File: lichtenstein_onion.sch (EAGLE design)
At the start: 40 parts, among them IC1 LM2852Y-3V3, J1 MAGJACK, U1 ONION-OMEGA2

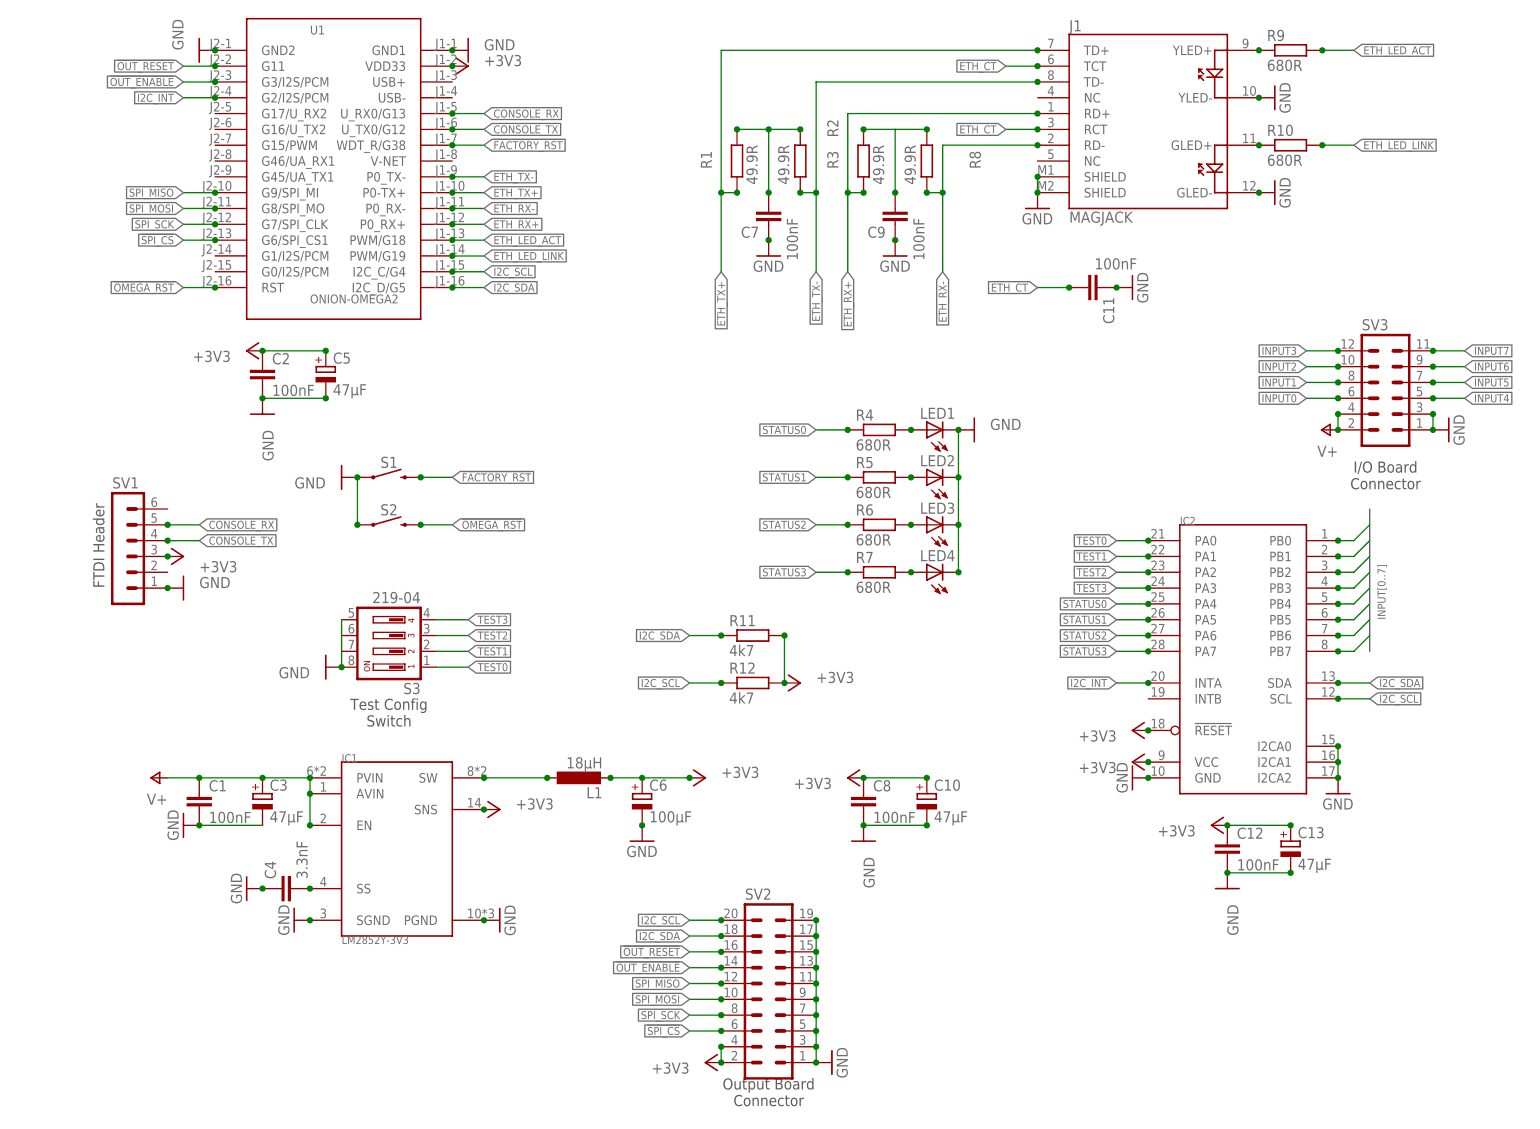
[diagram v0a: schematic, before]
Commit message: Added mouser part numbers for most components
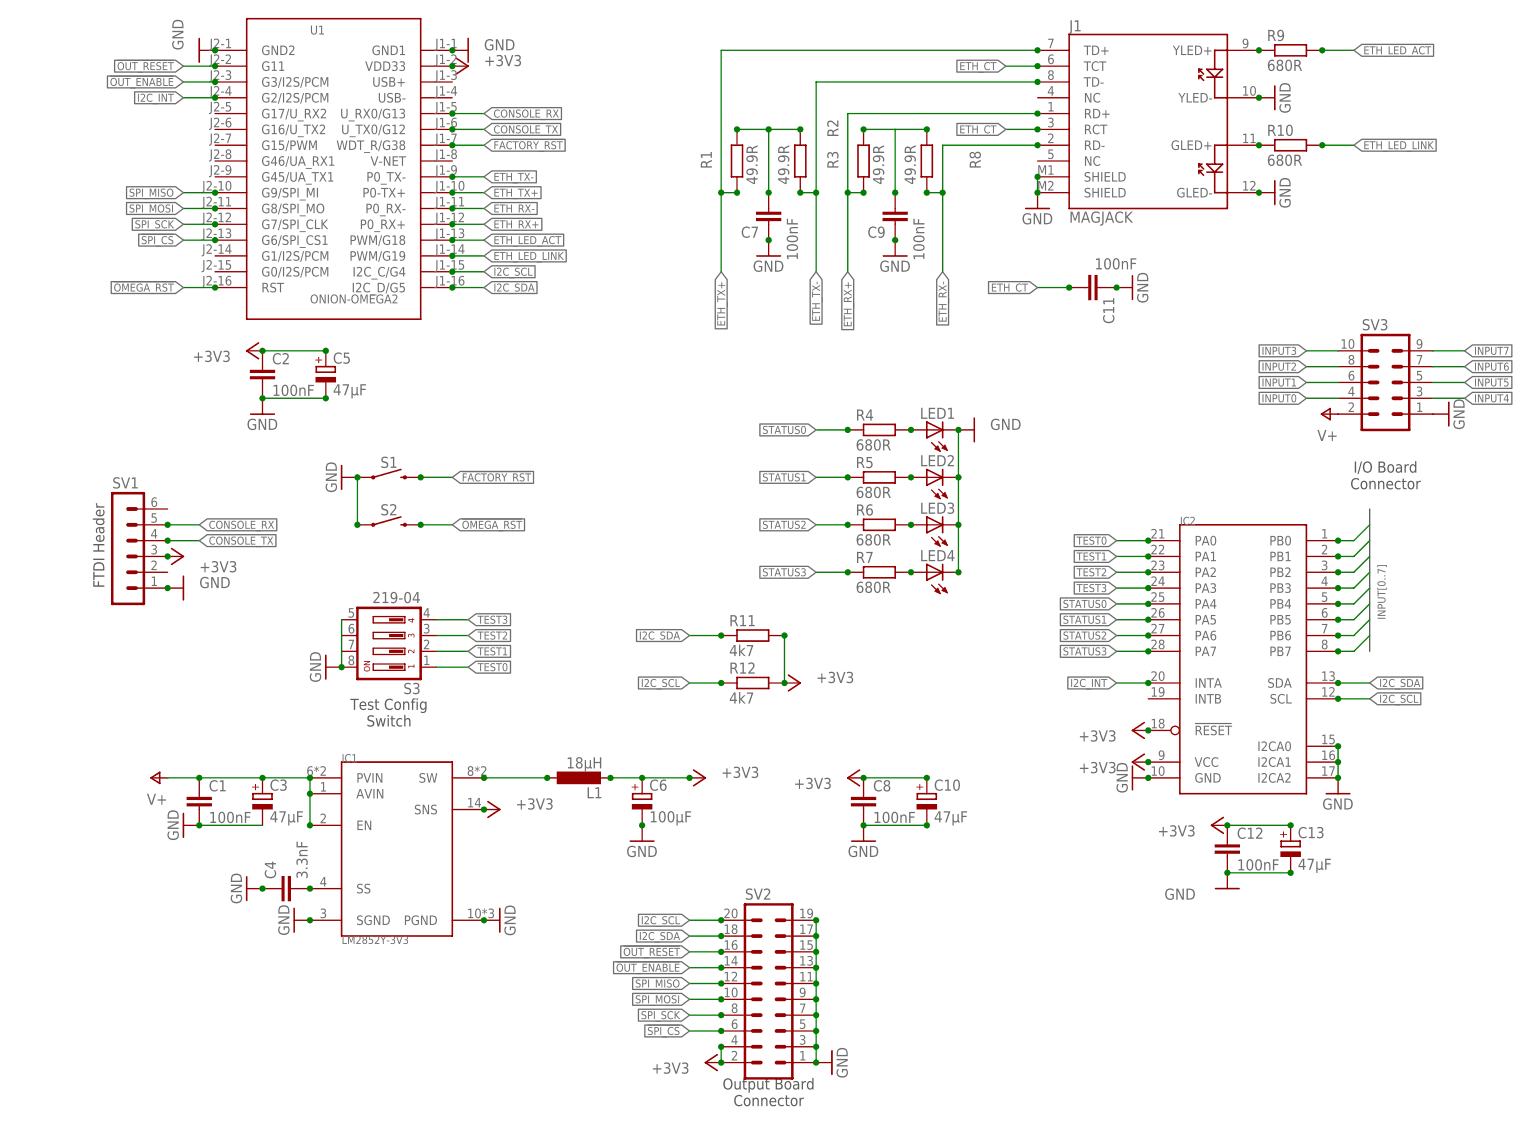
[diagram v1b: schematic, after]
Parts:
- C1, C11, C12, C2, C7, C8, C9: MOUSER (none) -> 710-885012207072
- C4: MOUSER (none) -> 710-885012207089
- L1: MOUSER SRR1050A-180Y -> (none)
- LED1: MOUSER (none) -> 604-APTR3216SRCPRV
- LED2, LED3, LED4: MOUSER (none) -> 604-APTR3216SGC
- R1, R11, R12, R2, R3, R8: MOUSER (none) -> 652-CR0805-FX4701GLF
- R10, R4, R5, R6, R7, R9: MOUSER (none) -> 652-CR0805-FX6800GLF
- S3: MOUSER (none) -> 774-219-4LPS
- SV2: MOUSER (none) -> 517-30320-6002
- SV3: device con-lstb:MA06-2 -> con-lstb:MA05-2; MOUSER (none) -> 517-30310-6002
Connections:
- net GND: no longer SV3.3
- net INPUT0: now also SV3.4; no longer SV3.6
- net INPUT1: now also SV3.6; no longer SV3.8
- net INPUT2: now also SV3.8; no longer SV3.10
- net INPUT3: now also SV3.10; no longer SV3.12
- net INPUT4: now also SV3.3; no longer SV3.5
- net INPUT5: now also SV3.5; no longer SV3.7
- net INPUT6: now also SV3.7; no longer SV3.9
- net INPUT7: now also SV3.9; no longer SV3.11
- net V+: no longer SV3.4

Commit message: began pcb layout for main board
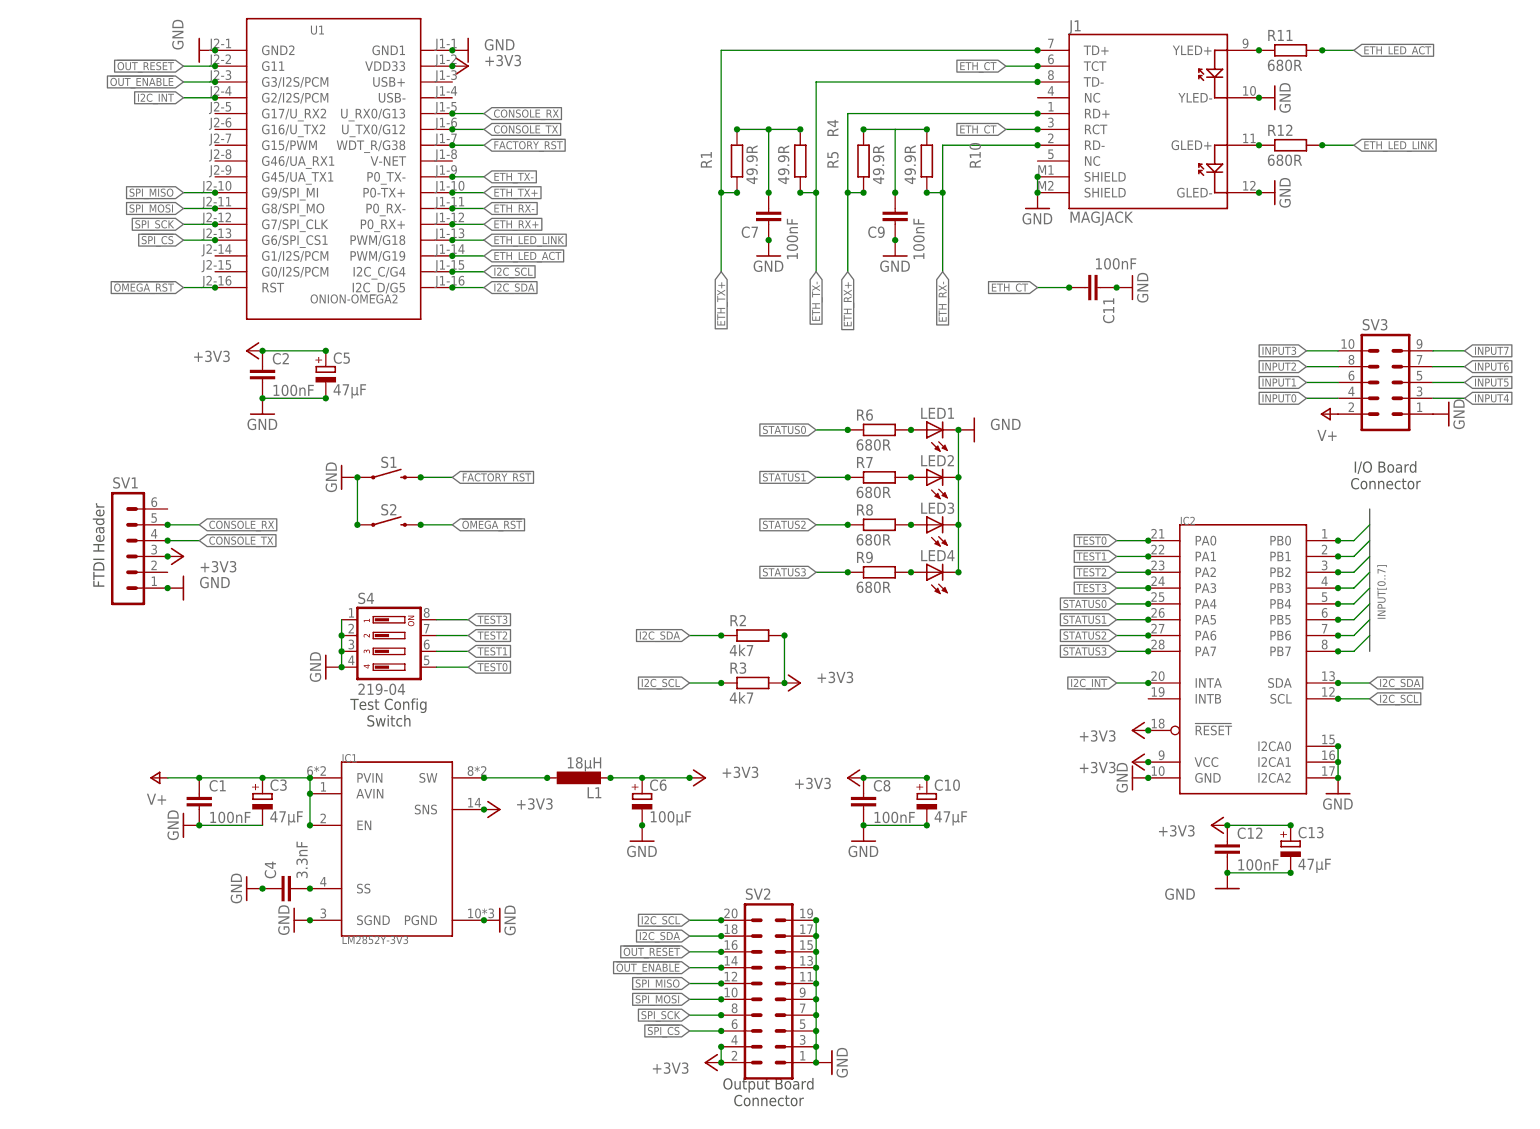
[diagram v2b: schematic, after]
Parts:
- removed S3: 219-04, switch-dil:219-04
- added S4: 219-04, switch-dil:219-04
- R10, R4, R5: value 680R -> 49.9R; MOUSER 652-CR0805-FX6800GLF -> 652-CR0805-FX4701GLF
- R11, R12: value 4k7 -> 680R; MOUSER 652-CR0805-FX4701GLF -> 652-CR0805-FX6800GLF
- R2, R3: value 49.9R -> 4k7
- R8: value 49.9R -> 680R; MOUSER 652-CR0805-FX4701GLF -> 652-CR0805-FX6800GLF
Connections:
- net +3V3: now also R2.2, R3.2; no longer R11.2, R12.2
- net ETH_LED_ACT: now also R11.2, U1.PWM/G19; no longer R9.2, U1.PWM/G18
- net ETH_LED_LINK: now also R12.2, U1.PWM/G18; no longer R10.2, U1.PWM/G19
- net ETH_RX+: now also R5.1; no longer R3.1
- net ETH_RX-: now also R10.1; no longer R8.1
- net ETH_TX-: now also R4.1; no longer R2.1
- net GND: now also S4.1, S4.2, S4.3, S4.4; no longer S3.5, S3.8
- net I2C_SCL: now also R3.1; no longer R12.1
- net I2C_SDA: now also R2.1; no longer R11.1
- net N$10: now also R8.2; no longer R6.2
- net N$11: now also R9.2; no longer R7.2
- net N$2: now also R6.2; no longer R4.2
- net N$3: now also R4.2; no longer R2.2
- net N$4: now also R11.1; no longer R9.1
- net N$5: now also R12.1; no longer R10.1
- net N$6: now also R10.2, R5.2; no longer R3.2, R8.2
- net N$9: now also R7.2; no longer R5.2
- net STATUS0: now also R6.1; no longer R4.1
- net STATUS1: now also R7.1; no longer R5.1
- net STATUS2: now also R8.1; no longer R6.1
- net STATUS3: now also R9.1; no longer R7.1
- net TEST0: now also S4.5; no longer S3.1
- net TEST1: now also S4.6; no longer S3.2
- net TEST2: now also S4.7; no longer S3.3
- net TEST3: now also S4.8; no longer S3.4
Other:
- moved on the sheet: R10, R11, R12, R2, R3, R4, R5, R6, R7, R8, R9

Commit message: finished main board layout
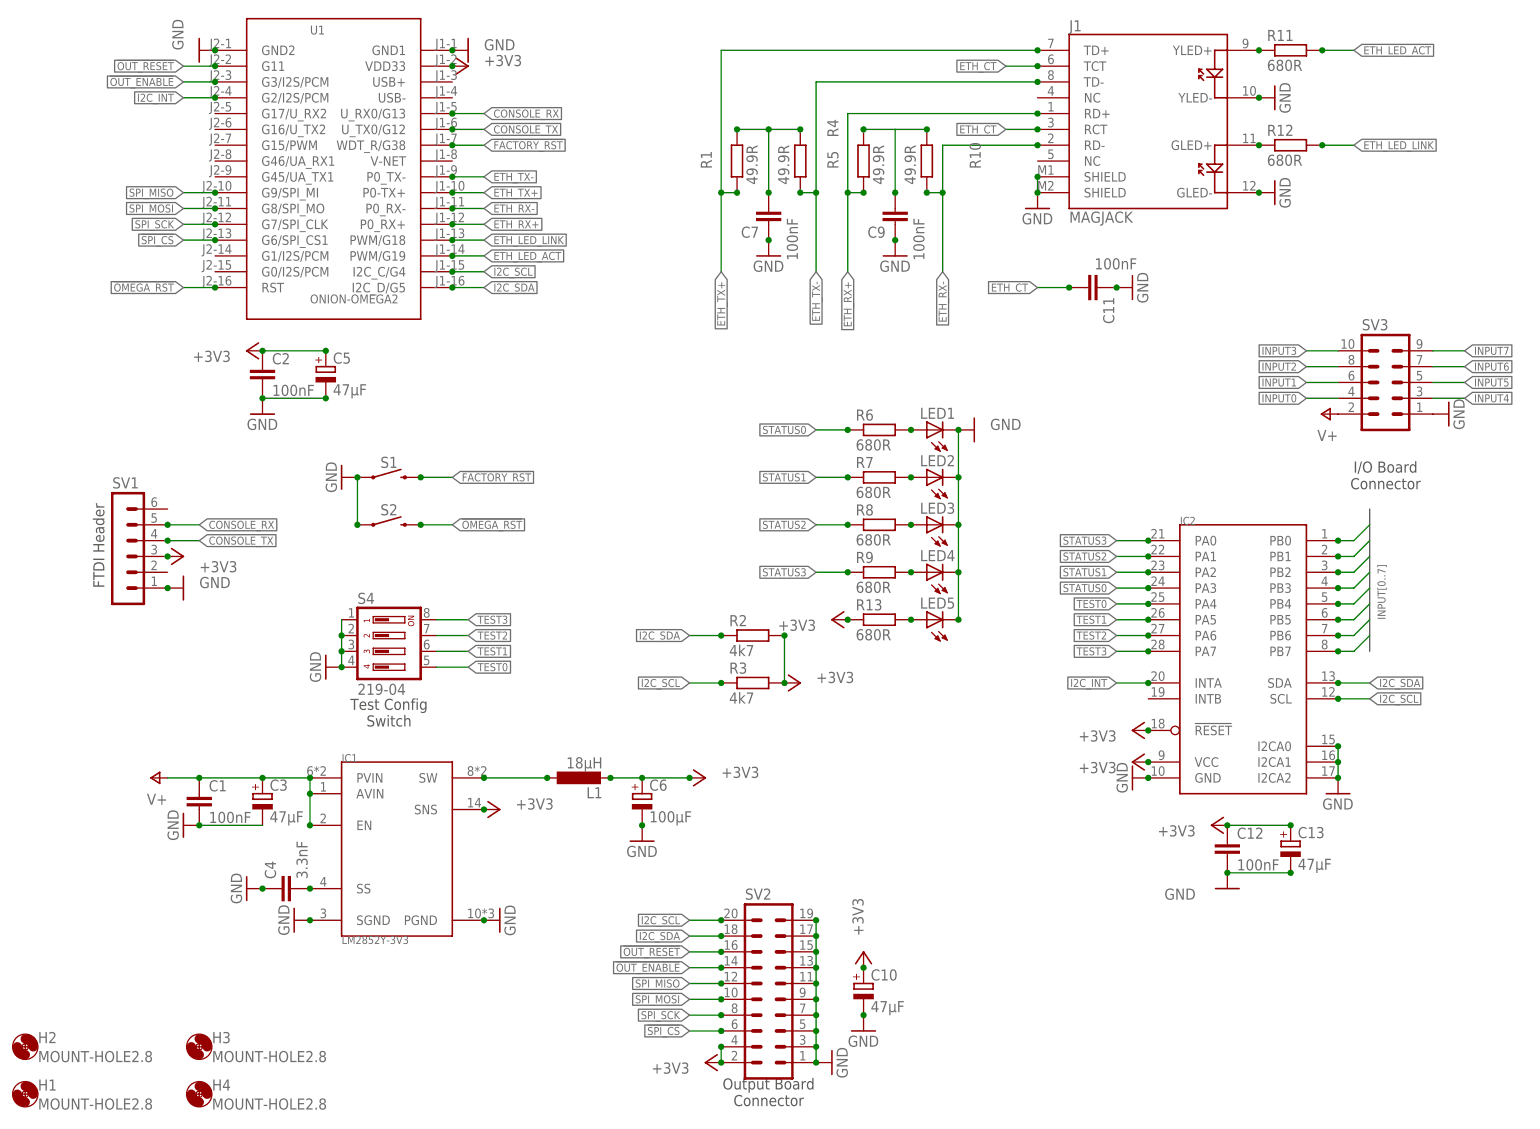
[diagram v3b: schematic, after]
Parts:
- removed C8: 100nF, rcl:C-EUC0805
- added H1, H2, H3, H4: MOUNT-HOLE2.8, holes:MOUNT-HOLE2.8
- added LED5: (no value), led:LEDCHIPLED_1206
- added R13: 680R, rcl:R-EU_M0805
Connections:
- new net N$1: LED5.A, R13.2
- net +3V3: now also R13.1; no longer C8.1
- net GND: now also LED5.C; no longer C8.2
- net INPUT0: now also IC2.PB1; no longer IC2.PB0
- net INPUT1: now also IC2.PB3; no longer IC2.PB1
- net INPUT2: now also IC2.PB5; no longer IC2.PB2
- net INPUT3: now also IC2.PB7; no longer IC2.PB3
- net INPUT4: now also IC2.PB0; no longer IC2.PB4
- net INPUT5: now also IC2.PB2; no longer IC2.PB5
- net INPUT6: now also IC2.PB4; no longer IC2.PB6
- net INPUT7: now also IC2.PB6; no longer IC2.PB7
- net STATUS0: now also IC2.PA3; no longer IC2.PA4
- net STATUS1: now also IC2.PA2; no longer IC2.PA5
- net STATUS2: now also IC2.PA1; no longer IC2.PA6
- net STATUS3: now also IC2.PA0; no longer IC2.PA7
- net TEST0: now also IC2.PA4; no longer IC2.PA0
- net TEST1: now also IC2.PA5; no longer IC2.PA1
- net TEST2: now also IC2.PA6; no longer IC2.PA2
- net TEST3: now also IC2.PA7; no longer IC2.PA3
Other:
- moved on the sheet: C10

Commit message: Rev01 sent to manufacture
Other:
- moved on the sheet: C10, SV2

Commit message: BOM for base board
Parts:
- S1, S2: MOUSER (none) -> 612-TL1105B
- U1: MOUSER (none) -> 353-OM-O2P
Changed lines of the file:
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@@
 <parts>
 <part name="FRAME1" library="frames" library_urn="urn:adsk.eagle:library:229" deviceset="LETTER_L" device=""/>
-<part name="U1" library="lichtenstein_onion" deviceset="ONION-OMEGA2" device=""/>
+<part name="U1" library="lichtenstein_onion" deviceset="ONION-OMEGA2" device="">
+<attribute name="MOUSER" value="353-OM-O2P"/>
+</part>
 <part name="+3V33" library="supply1" library_urn="urn:adsk.eagle:library:371" deviceset="+3V3" device=""/>
 <part name="GND9" library="supply1" library_urn="urn:adsk.eagle:library:371" deviceset="GND" device=""/>
@@
 <part name="GND24" library="supply1" library_urn="urn:adsk.eagle:library:371" deviceset="GND" device=""/>
 <part name="P+2" library="supply1" library_urn="urn:adsk.eagle:library:371" deviceset="V+" device=""/>
-<part name="S1" library="SparkFun-Switches" deviceset="MOMENTARY-SWITCH-SPST" device="-PTH-6.0MM" value=""/>
-<part name="S2" library="SparkFun-Switches" deviceset="MOMENTARY-SWITCH-SPST" device="-PTH-6.0MM" value=""/>
+<part name="S1" library="SparkFun-Switches" deviceset="MOMENTARY-SWITCH-SPST" device="-PTH-6.0MM" value="">
+<attribute name="MOUSER" value="612-TL1105B"/>
+</part>
+<part name="S2" library="SparkFun-Switches" deviceset="MOMENTARY-SWITCH-SPST" device="-PTH-6.0MM" value="">
+<attribute name="MOUSER" value="612-TL1105B"/>
+</part>
 <part name="GND7" library="supply1" library_urn="urn:adsk.eagle:library:371" deviceset="GND" device=""/>
 <part name="LED1" library="led" library_urn="urn:adsk.eagle:library:259" deviceset="LED" device="CHIPLED_1206" package3d_urn="urn:adsk.eagle:package:15823/2">
@@
 <instance part="FRAME1" gate="G$1" x="0" y="0"/>
 <instance part="FRAME1" gate="G$2" x="147.32" y="0"/>
-<instance part="U1" gate="G$1" x="58.42" y="157.48"/>
+<instance part="U1" gate="G$1" x="58.42" y="157.48">
+<attribute name="MOUSER" x="58.42" y="157.48" size="1.27" layer="96" display="off"/>
+</instance>
 <instance part="+3V33" gate="G$1" x="76.2" y="170.18" smashed="yes" rot="R270">
 <attribute name="VALUE" x="78.74" y="170.18" size="1.778" layer="96"/>
@@
 <instance part="GND24" gate="1" x="233.68" y="114.3" rot="R90"/>
 <instance part="P+2" gate="1" x="213.36" y="114.3" rot="R90"/>
-<instance part="S1" gate="G$1" x="63.5" y="104.14"/>
-<instance part="S2" gate="G$1" x="63.5" y="96.52"/>
+<instance part="S1" gate="G$1" x="63.5" y="104.14">
+<attribute name="MOUSER" x="63.5" y="104.14" size="1.27" layer="96" display="off"/>
+</instance>
+<instance part="S2" gate="G$1" x="63.5" y="96.52">
+<attribute name="MOUSER" x="63.5" y="96.52" size="1.27" layer="96" display="off"/>
+</instance>
 <instance part="GND7" gate="1" x="53.34" y="73.66" rot="R270"/>
 <instance part="LED1" gate="G$1" x="149.86" y="111.76" rot="R90">
@@
 <pinref part="GND2" gate="1" pin="GND"/>
 <junction x="33.02" y="48.26"/>
+<junction x="43.18" y="48.26"/>
 </segment>
 <segment>
@@
 <pinref part="S4" gate="G$1" pin="4"/>
 <junction x="55.88" y="73.66"/>
+<junction x="55.88" y="81.28"/>
 </segment>
 <segment>
@@
 <label x="76.2" y="81.28" size="1.27" layer="95" xref="yes"/>
 <pinref part="S4" gate="G$1" pin="8"/>
+<junction x="71.12" y="81.28"/>
 </segment>
 <segment>
@@
 <label x="76.2" y="78.74" size="1.27" layer="95" xref="yes"/>
 <pinref part="S4" gate="G$1" pin="7"/>
+<junction x="71.12" y="78.74"/>
 </segment>
 <segment>
@@
 <label x="76.2" y="76.2" size="1.27" layer="95" xref="yes"/>
 <pinref part="S4" gate="G$1" pin="6"/>
+<junction x="71.12" y="76.2"/>
 </segment>
 <segment>
@@
 <label x="76.2" y="73.66" size="1.27" layer="95" xref="yes"/>
 <pinref part="S4" gate="G$1" pin="5"/>
-</segment>
-<segment>
+<junction x="71.12" y="73.66"/>
+</segment>
+<segment>
